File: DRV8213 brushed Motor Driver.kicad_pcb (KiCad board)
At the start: 4 copper layers, 15 x 15 mm, 27 parts, among them J1 Keystone 6102, J10 Precidip 852-10-004-20-001101, J11 Precidip 852-10-004-20-001101, J2 Keystone 6102, J3 Keystone 6100, J4 Keystone 6100, J5 Keystone 6102, J6 Keystone 6102, J7 Keystone 6100, J8 Keystone 6100, J9 JST PH 2mm horizontal, U1 DRV8213RTER, U2 LP2981-3.3

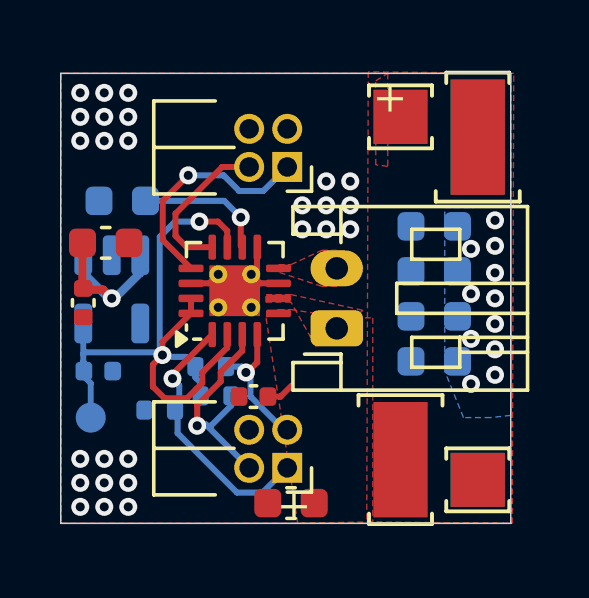
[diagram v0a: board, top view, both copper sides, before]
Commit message: Reversed connector pin assignments to mirror hub
Technically any pin would work, but I want it logical order with A matching with A. Some hubs may not have enough pins also, so most important pins go first. I might change the footprint numbers to match as well, but this is less important.
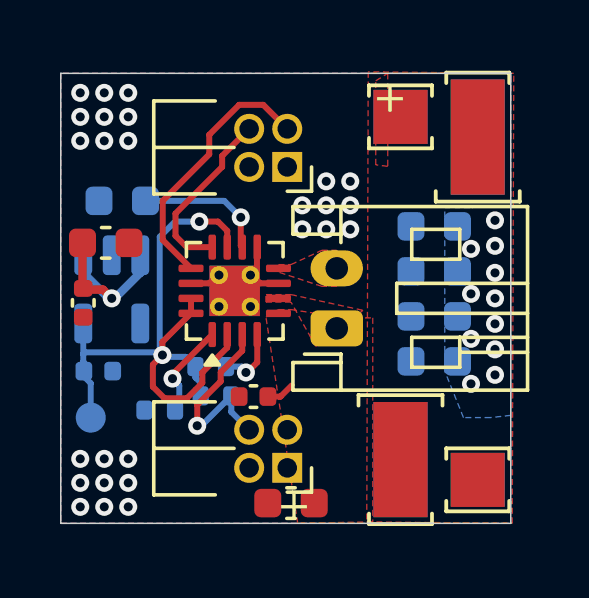
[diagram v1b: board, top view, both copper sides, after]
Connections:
- J10 pad 1: PWM-A -> unconnected-(J10-Pin_1-Pad1)
- J10 pad 2: PWM-B -> unconnected-(J10-Pin_2-Pad2)
- J10 pad 3: unconnected-(J10-Pin_3-Pad3) -> PWM-A
- J10 pad 4: unconnected-(J10-Pin_4-Pad4) -> PWM-B
- J11 pad 1: ADC-A -> Fault
- J11 pad 2: Stall -> unconnected-(J11-Pin_2-Pad2)
- J11 pad 3: Fault -> ADC-A
- J11 pad 4: unconnected-(J11-Pin_4-Pad4) -> Stall
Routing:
- net Fault: track 4.81 -> 7.33 mm
- net Stall: track 7.74 -> 6.59 mm
- net PWM-A: track 7.69 -> 8.83 mm, vias 1 -> 0
- net ADC-A: track 8.93 -> 8.10 mm
- net PWM-B: track 5.22 -> 5.96 mm

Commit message: Fixed Silkscreen
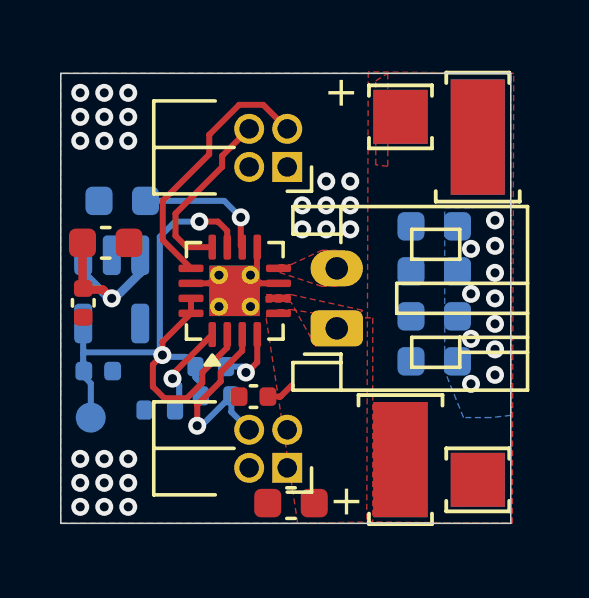
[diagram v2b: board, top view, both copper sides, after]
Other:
- board text added: "A"
- board text added: "A B"
- board text added: "Stall"
- board text removed: "rush"
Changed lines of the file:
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@@
 	)
 	(gr_line
-		(start 169.1 105.4)
-		(end 169.9 104.7)
+		(start 172.025 108.825)
+		(end 171.325 108.025)
+		(stroke
+			(width 0.12)
+			(type default)
+		)
+		(layer "B.SilkS")
+	)
+	(gr_line
+		(start 171.35 105.45)
+		(end 171.425 104.6)
+		(stroke
+			(width 0.12)
+			(type default)
+		)
+		(layer "B.SilkS")
+	)
+	(gr_line
+		(start 170.275 105.4)
+		(end 170.075 103.35)
 		(stroke
 			(width 0.12)
@@
 	)
 	(gr_text "+"
-		(at 174.2 95.6 -0)
+		(at 172.575 95.4 -0)
 		(layer "F.SilkS")
 		(effects
@@
 	)
 	(gr_text "+"
-		(at 171 109.2 -0)
+		(at 172.75 109.025 -0)
 		(layer "F.SilkS")
 		(effects
@@
 		)
 	)
+	(gr_text "A"
+		(at 172.225 104.65 90)
+		(layer "B.SilkS")
+		(effects
+			(font
+				(size 1 1)
+				(thickness 0.15)
+			)
+			(justify right bottom mirror)
+		)
+	)
+	(gr_text "Stall"
+		(at 170.55 103.175 0)
+		(layer "B.SilkS")
+		(effects
+			(font
+				(size 1 1)
+				(thickness 0.15)
+			)
+			(justify left bottom mirror)
+		)
+	)
 	(gr_text "<20A"
-		(at 174.8 99.1 0)
+		(at 174.75 99.35 0)
 		(layer "B.SilkS")
 		(effects
@@
 	)
 	(gr_text "Fault"
-		(at 173.2 104.6 0)
+		(at 173.4 105.175 90)
 		(layer "B.SilkS")
 		(effects
@@
 	)
 	(gr_text "PWM"
-		(at 167.3 96.6 0)
+		(at 168.075 94.225 90)
 		(layer "B.SilkS")
 		(effects
@@
 		)
 	)
-	(gr_text "B A"
-		(at 170.35 98.65 90)
+	(gr_text "A B"
+		(at 169.225 95.425 0)
 		(layer "B.SilkS")
 		(effects
@@
 	)
 	(gr_text "-"
-		(at 175.1 109.1 -0)
+		(at 178.75 106.7 -0)
 		(layer "B.SilkS")
 		(effects
@@
 	)
 	(gr_text "CSA"
-		(at 170.2 105.6 90)
-		(layer "B.SilkS")
-		(effects
-			(font
-				(size 1 1)
-				(thickness 0.15)
-			)
-			(justify left bottom mirror)
-		)
-	)
-	(gr_text "rush"
-		(at 170.45 99.85 0)
+		(at 168.625 106.15 90)
 		(layer "B.SilkS")
 		(effects
@@
 	)
 	(gr_text "-"
-		(at 175.9 95.3 -0)
+		(at 175.75 97.95 -0)
 		(layer "B.SilkS")
 		(effects
@@
 		)
 	)
-	(gr_text_box "3.7~7.4V"
-		(start 176.825 98.1492)
-		(end 178.975 104.7)
+	(gr_text_box "3.0~12V"
+		(start 176.825 98.6742)
+		(end 178.975 105.225)
 		(margins 0.75 0.75 0.75 0.75)
 		(angle 90)

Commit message: Tweaked silkscreen and via placement
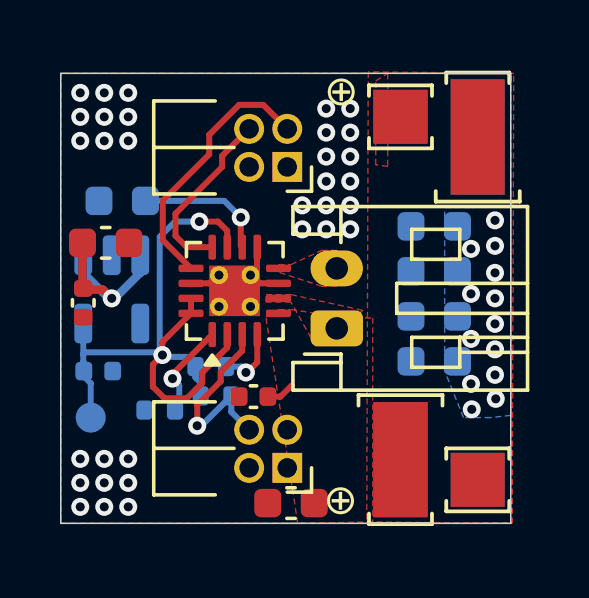
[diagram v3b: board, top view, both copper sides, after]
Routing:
- net VDD: vias 12 -> 14
- net GNDPWR: vias 26 -> 32
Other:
- board text added: "⊕"
- board text added: "⊖"
- board text removed: "+"
- board text removed: "-"
- board text removed: "A"
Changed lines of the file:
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@@
 	)
 	(gr_line
-		(start 172.025 108.825)
+		(start 170.775 108.825)
 		(end 171.325 108.025)
 		(stroke
@@
 		(layer "Edge.Cuts")
 	)
-	(gr_text "+"
-		(at 172.575 95.4 -0)
+	(gr_text "⊕"
+		(at 172.575 95.375 0)
 		(layer "F.SilkS")
 		(effects
@@
 		)
 	)
-	(gr_text "+"
-		(at 172.75 109.025 -0)
+	(gr_text "⊕"
+		(at 172.55 109 0)
 		(layer "F.SilkS")
 		(effects
@@
 			)
 			(justify left bottom)
-		)
-	)
-	(gr_text "A"
-		(at 172.225 104.65 90)
-		(layer "B.SilkS")
-		(effects
-			(font
-				(size 1 1)
-				(thickness 0.15)
-			)
-			(justify right bottom mirror)
 		)
 	)
@@
 	)
 	(gr_text "Fault"
-		(at 173.4 105.175 90)
+		(at 170.75 109.1 0)
 		(layer "B.SilkS")
 		(effects
@@
 		)
 	)
-	(gr_text "-"
-		(at 178.75 106.7 -0)
+	(gr_text "⊖"
+		(at 173.937583 108.991882 0)
 		(layer "B.SilkS")
 		(effects
@@
 	)
 	(gr_text "CSA"
-		(at 168.625 106.15 90)
-		(layer "B.SilkS")
-		(effects
-			(font
-				(size 1 1)
-				(thickness 0.15)
-			)
-			(justify left bottom mirror)
-		)
-	)
-	(gr_text "-"
-		(at 175.75 97.95 -0)
-		(layer "B.SilkS")
-		(effects
-			(font
-				(size 1 1)
-				(thickness 0.15)
-			)
-			(justify left bottom mirror)
-		)
-	)
-	(gr_text_box "3.0~12V"
+		(at 174.4 104.725 0)
+		(layer "B.SilkS")
+		(effects
+			(font
+				(size 1 1)
+				(thickness 0.15)
+			)
+			(justify left bottom mirror)
+		)
+	)
+	(gr_text "⊖"
+		(at 173.967836 95.373351 0)
+		(layer "B.SilkS")
+		(effects
+			(font
+				(size 1 1)
+				(thickness 0.15)
+			)
+			(justify left bottom mirror)
+		)
+	)
+	(gr_text_box "3.0~11V"
 		(start 176.825 98.6742)
 		(end 178.975 105.225)
@@
 	)
 	(via
+		(at 178.3 105.05)
+		(size 0.6)
+		(drill 0.3)
+		(layers "F.Cu" "B.Cu")
+		(free yes)
+		(net 1)
+	)
+	(via
 		(at 177.475 100.05)
+		(size 0.6)
+		(drill 0.3)
+		(layers "F.Cu" "B.Cu")
+		(free yes)
+		(net 1)
+	)
+	(via
+		(at 177.5 105.4)
 		(size 0.6)
 		(drill 0.3)
@@
 	)
 	(via
+		(at 173.45 95.375)
+		(size 0.6)
+		(drill 0.3)
+		(layers "F.Cu" "B.Cu")
+		(free yes)
+		(net 2)
+	)
+	(via
+		(at 172.65 95.375)
+		(size 0.6)
+		(drill 0.3)
+		(layers "F.Cu" "B.Cu")
+		(free yes)
+		(net 2)
+	)
+	(via
+		(at 172.65 96.175)
+		(size 0.6)
+		(drill 0.3)
+		(layers "F.Cu" "B.Cu")
+		(free yes)
+		(net 2)
+	)
+	(via
+		(at 173.45 96.975)
+		(size 0.6)
+		(drill 0.3)
+		(layers "F.Cu" "B.Cu")
+		(free yes)
+		(net 2)
+	)
+	(via
 		(at 173.45 97.8)
 		(size 0.6)
@@
 	)
 	(via
+		(at 172.65 96.975)
+		(size 0.6)
+		(drill 0.3)
+		(layers "F.Cu" "B.Cu")
+		(free yes)
+		(net 2)
+	)
+	(via
 		(at 165.25 95.65)
 		(size 0.6)
@@
 		(size 0.6)
 		(drill 0.3)
+		(layers "F.Cu" "B.Cu")
+		(free yes)
+		(net 2)
+	)
+	(via
+		(at 173.45 96.175)
+		(size 0.6)
+		(drill 0.3)
